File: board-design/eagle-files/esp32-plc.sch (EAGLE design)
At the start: 42 parts, among them P1 47346-0001, Q1 600mA/40V, Q2 600mA/40V, U1 ESP32-WROOM-32D, U2 FT231XS, U3 BD48E27G-TR, U5 EC20CEFASG-MINIPCIE

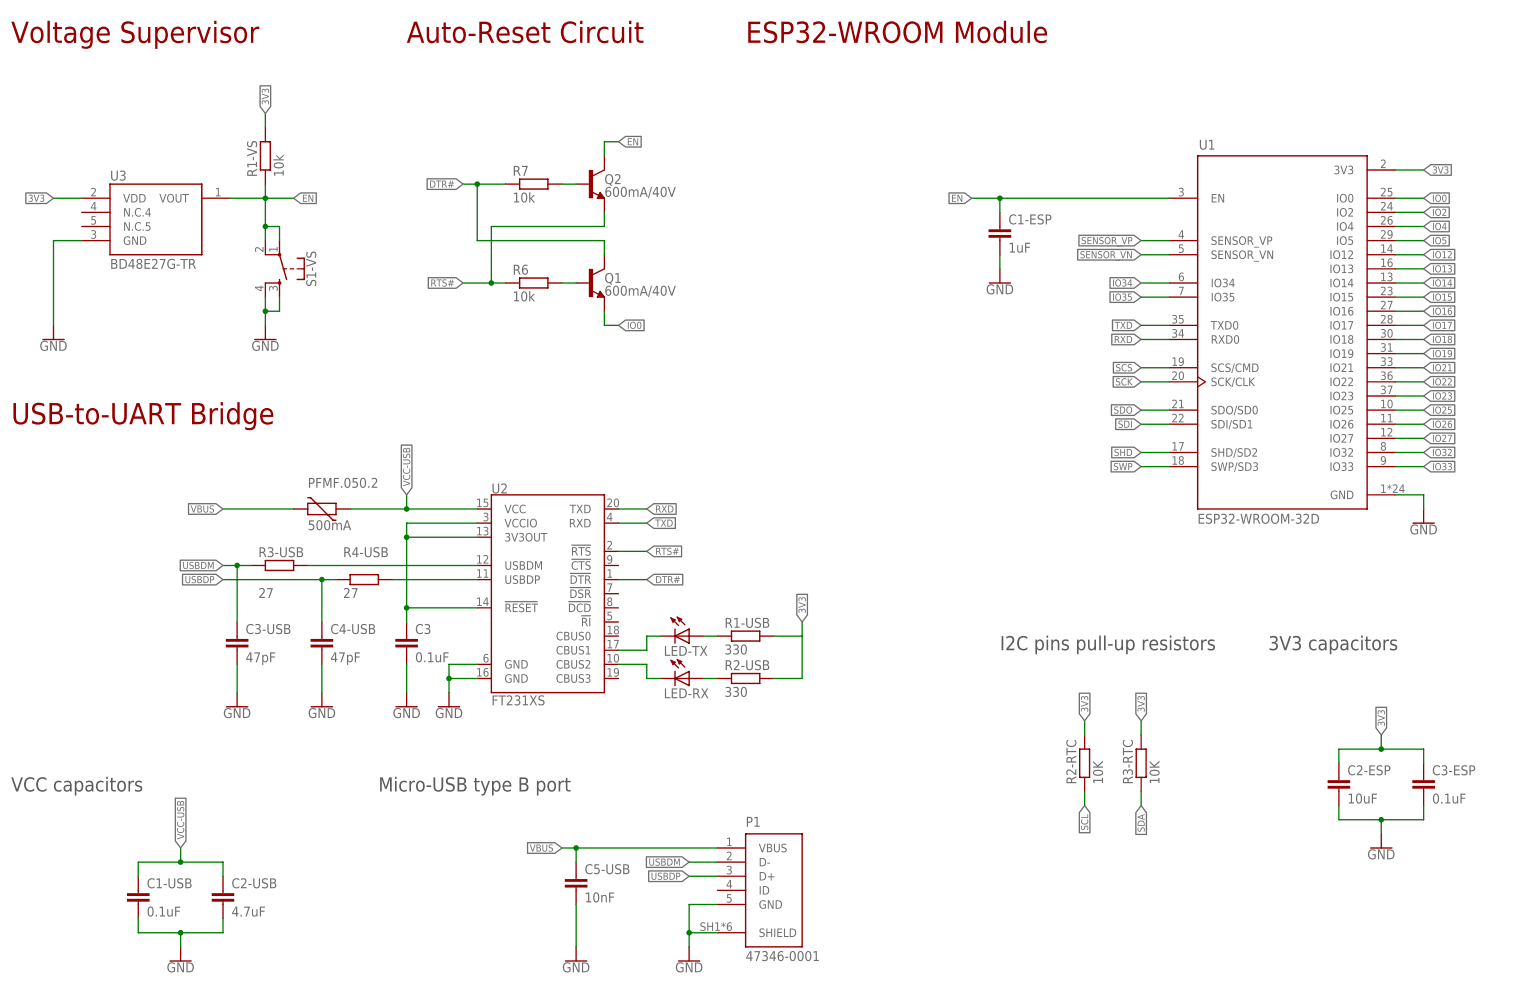
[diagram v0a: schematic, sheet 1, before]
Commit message: Changed board schematic
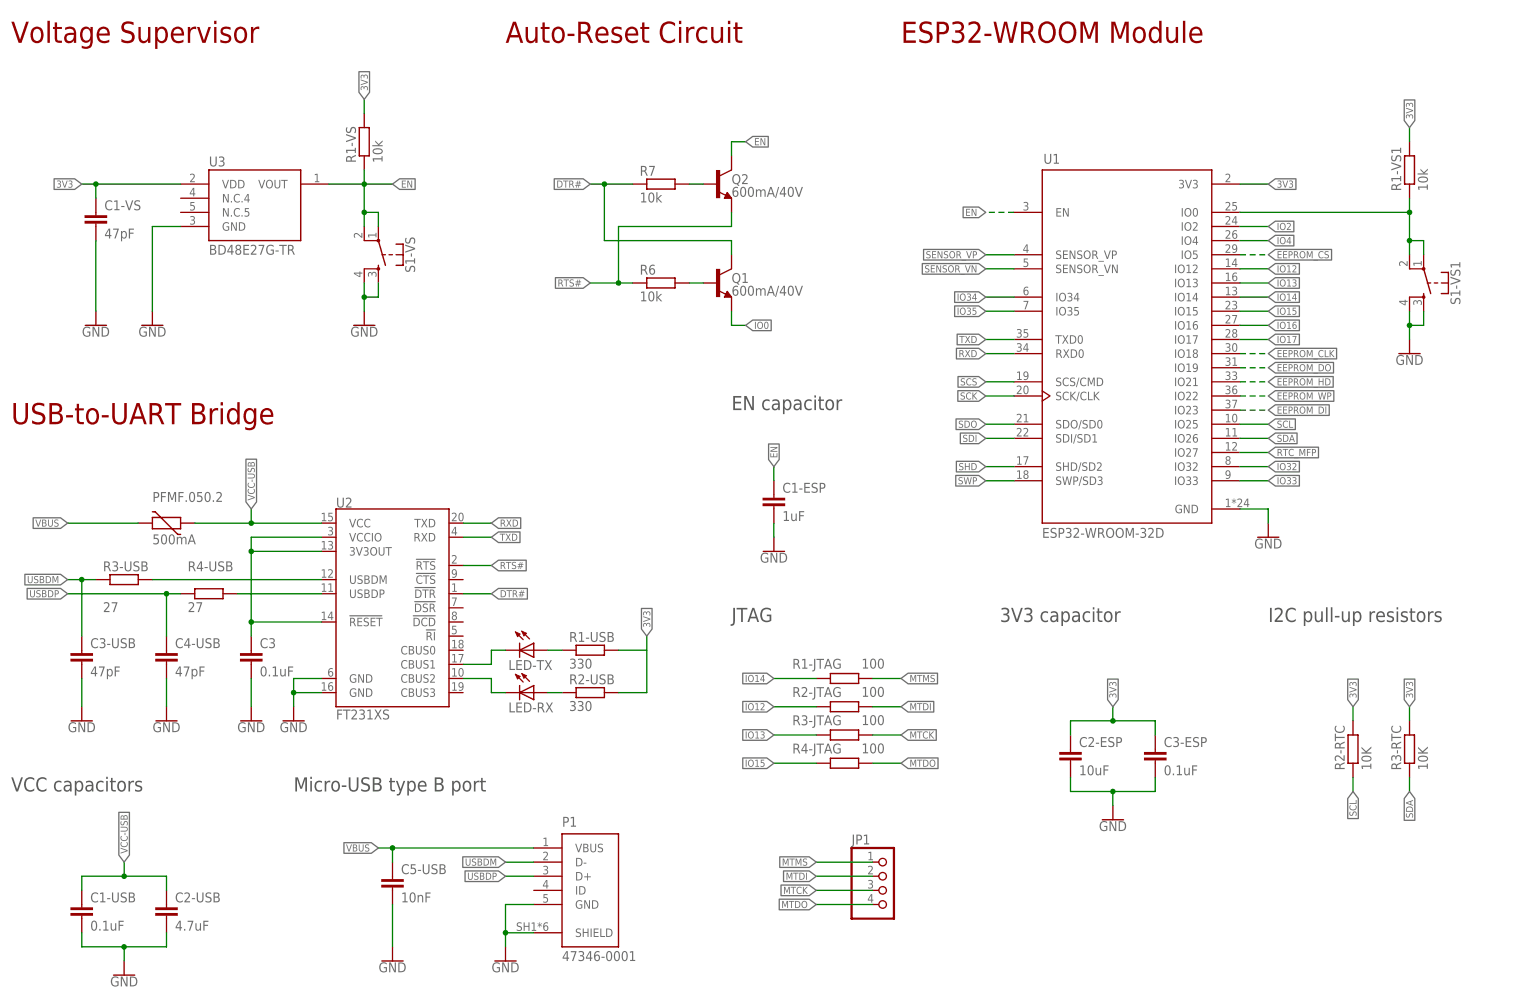
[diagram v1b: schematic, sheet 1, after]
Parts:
- removed C1-PWR: 100uF, rcl:C-EUC0402
- removed C2-PWR: 1000uF, rcl:C-EUC0402
- added C1-VS: 47pF, rcl:C-EUC0402
- added C2: 1000uF, cap-pan40:C-PR-5,0X10
- added C4: 100uF, cap-pan40:C-PR-5,0X10
- added JP1: (no value), pinhead:PINHD-1X4
- added R1-JTAG, R2-JTAG, R3-JTAG, R4-JTAG: 100, rcl:R-EU_R0402
- added R1-VS1: 10k, rcl:R-EU_R0402
- added S1-VS1: (no value), SparkFun-Switches:MOMENTARY-SWITCH-SPST-2-SMD-4.6X2.8MM
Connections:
- net N$14 renamed STATUS
- net N$15 renamed VBAT_BB
- net N$16 renamed VBAT_RF
- net N$17 renamed ANT_DIV
- net N$18 renamed ANT_MAIN
- net N$19 renamed ANT_GNSS
- net N$2 renamed USB_VBUS
- net N$20 renamed ADC0
- net N$21 renamed ADC1
- net N$22 renamed I2C_SDA
- net N$23 renamed I2C_SCL
- net N$24 renamed VDD_EXT
- net N$25 renamed AP_READY
- net N$26 renamed W_DISABLE#
- net N$27 renamed NET_MODE
- net N$28 renamed NET_STATUS
- net N$39 renamed WAKEUP_IN
- net N$40 renamed DBG_RXD
- net N$41 renamed DBG_TXD
- net N$42 renamed USIM_VDD
- net N$43 renamed USIM_GND
- net N$44 renamed USIM_DATA
- net N$45 renamed USIM_CLK
- net N$46 renamed USIM_RST
- net N$47 renamed RESET_IN
- net N$48 renamed PWRKEY
- net N$49 renamed PCM_IN
- net N$5 renamed USB_DM
- net N$50 renamed PCM_OUT
- net N$51 renamed PCM_SYNC
- net N$52 renamed PCM_CLK
- net N$53 renamed RESERVED
- net N$6 renamed USB_DP
- removed net IO18: U1.IO18
- removed net IO19: U1.IO19
- removed net IO21: U1.IO21
- removed net IO22: U1.IO22
- removed net IO23: U1.IO23
- removed net IO25: U1.IO25
- removed net IO26: U1.IO26
- removed net IO27: U1.IO27
- removed net IO5: U1.IO5
- removed net N$54: U5.GND
- new net MTCK: JP1.3, R3-JTAG.2
- new net MTDI: JP1.2, R2-JTAG.2
- new net MTDO: JP1.4, R4-JTAG.2
- new net MTMS: JP1.1, R1-JTAG.2
- new net VIN: C4.+, U$2.VIN
- net 3V3: now also C1-VS.1, C2.+, R1-VS1.2; no longer C2-PWR.1
- net EEPROM_CLK: now also U1.IO18
- net EEPROM_CS: now also U1.IO5
- net EEPROM_DI: now also U1.IO23
- net EEPROM_DO: now also U1.IO19
- net EEPROM_HD: now also U1.IO21
- net EEPROM_WP: now also U1.IO22
- net GND: now also C1-VS.2, C2.-, C4.-, S1-VS1.3, S1-VS1.4, U5.GND; no longer C1-PWR.2, C2-PWR.2
- net IO0: no longer U1.IO0
- net IO12: now also R2-JTAG.1
- net IO13: now also R3-JTAG.1
- net IO14: now also R1-JTAG.1
- net IO15: now also R4-JTAG.1
- net N$1: now also R1-VS1.1, S1-VS1.1, S1-VS1.2, U1.IO0; no longer C1-PWR.1, U$2.VIN
- net RTC_MFP: now also U1.IO27
- net SCL: now also U1.IO25
- net SDA: now also U1.IO26
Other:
- note added: "3V3 capacitor"
- note added: "EC20 LTE Cat 4 Module"
- note added: "EN capacitor"
- note added: "I2C pull-up resistors"
- note added: "JTAG"
- note added: "Transistor / IC translation for UART communication required (IC translation recommended - IC needed) Further footprint checks required (2019 hardware manual for reference) Version R2.1: https://ro.mouser.com/datasheet/2/1052/Quectel_EC20_R2.1_LTE_Specification_V1.2-1830665.pdf"
- note removed: "3V3 capacitors"
- note removed: "I2C pins pull-up resistors"
- moved on the sheet: C1-EEPROM, C1-ESP, C1-USB, C2-ESP, C2-USB, C3, C3-ESP, C3-USB, C4-USB, C5-USB, LED-RX, LED-TX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

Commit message: Eagle schematic changed
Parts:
- removed C1-EEPROM, C3-RTC: 100nF, rcl:C-EUC0402
- removed C1-ESP: 1uF, rcl:C-EUC0402
- removed C1-RTC, C2-RTC: 5pF, rcl:C-EUC0402
- removed C1-USB, C3, C3-ESP: 0.1uF, rcl:C-EUC0402
- removed C1-VS, C3-USB, C4-USB: 47pF, rcl:C-EUC0402
- removed C2: 1000uF, cap-pan40:C-PR-5,0X10
- removed C2-ESP: 10uF, rcl:C-EUC0402
- removed C2-USB: 4.7uF, rcl:C-EUC0402
- removed C4: 100uF, cap-pan40:C-PR-5,0X10
- removed C5-USB: 10nF, rcl:C-EUC0402
- removed JP1: (no value), pinhead:PINHD-1X4
- removed LED-RX, LED-TX: (no value), adafruit:LEDCHIP-LED0603
- removed P1: 47346-0001, 47346-0001:47346-0001
- removed PFMF.050.2: 500mA, varistor:VARISTORCN1812
- removed R1-JTAG, R2-JTAG, R3-JTAG, R4-JTAG: 100, rcl:R-EU_R0402
- removed R1-USB, R2-USB: 330, rcl:R-EU_R0402
- removed R1-VS, R1-VS1, R6, R7: 10k, rcl:R-EU_R0402
- removed R2-RTC, R3-RTC: 10K, rcl:R-EU_R0402
- removed R3-USB, R4-USB: 27, rcl:R-EU_R0402
- removed S1-VS, S1-VS1: (no value), SparkFun-Switches:MOMENTARY-SWITCH-SPST-2-SMD-4.6X2.8MM
- removed U1: ESP32-WROOM-32D, ESP32-WROOM-32D:ESP32-WROOM-32D
- removed U2: FT231XS, SparkFun-IC-Comms:FT231XS
- removed U3: BD48E27G-TR, BD48E27G-TR:BD48E27G-TR
- removed U5: EC20CEFASG-MINIPCIE, Quectel:EC20CEFASG-MINIPCIE
- added C4-RTC: 100pF, rcl:C-EUC0402
- added D1: 24V, SparkFun-DiscreteSemi:DIODE_TVS
- added D2, D3: 3A/40V/500mV, SparkFun-DiscreteSemi:DIODE-SCHOTTKY-B340A
- added EEPROM-C1, EERAM-C1, ETH-VDD1A-C2, ETH-VDD2A-C2, ETH-VDDIO-C2, LTE-USIM-C1, LTE-VBAT-C2, LTE-VBAT-C6, PSU-OUT-C6, RTC-C1: 100nF, rcl:C-EUC0402
- added EERAM-C2: 33uF / 6.3V, rcl:C-EUC0402
- added ESP-C1: 22uF, rcl:C-EUC0402
- added ESP-C2: 0.1uF, rcl:C-EUC0402
- added ESP-C3, ETH-RJ45-C1, ETH-VDDCR-C1, VS-C1: 1uF, rcl:C-EUC0402
- added ESP-JTAG: (no value), pinhead:PINHD-1X4
- added ESP-R1, ESP-R2, ESP-R3, ESP-R4, ESP-R5, ESP-R6, ETH-RJ45-R10, ETH-RJ45-R9: 10k, rcl:R-EU_R0402
- added ESP-S1, ESP-S2: (no value), SparkFun-Switches:MOMENTARY-SWITCH-SPST-2-SMD-4.6X2.8MM
- added ESP-UART0: (no value), pinhead:PINHD-1X6
- added ETH-RJ45-R1, ETH-RJ45-R2, ETH-RJ45-R3, ETH-RJ45-R4: 49.9R, rcl:R-EU_R0402
- added ETH-RJ45-R5, ETH-RJ45-R6, R1-RTC1: 1k, rcl:R-EU_R0402
- added ETH-RJ45-R7: 12.1R (1%), rcl:R-EU_R0402
- added ETH-RJ45-R8: 500R, rcl:R-EU_R0402
- added ETH-VDD1A-C1, ETH-VDD2A-C1, PSU-IN-C3: 10uF, rcl:C-EUC0402
- added ETH-VDD2A-C3, ETH-VDD2A-C4, ETH-VDD2A-C5: 20pF, rcl:C-EUC0402
- added ETH-VDDCR-C2: 470pF, rcl:C-EUC0402
- added ETH-VDDIO-C1, LTE-VBAT-C10, LTE-VBAT-C9, PSU-OUT-C3: 22uF, rcl:CPOL-EUC/6032-28R
- added FB1: 30Ω/1.8A, SparkFun-Coils:FERRITE_BEAD-0603
- added G1: CR2032H, battery:CR2032H
- added L1: 330uH, rcl:L-EUL1812
- added L2, L3, L4: (no value), SparkFun-Coils:INDUCTOR
- added LTE-USIM-C2, LTE-USIM-C3, LTE-USIM-C4, LTE-VBAT-C3, LTE-VBAT-C7: 33pF, rcl:C-EUC0402
- added LTE-USIM-R1: 15K, rcl:R-EU_R0402
- added LTE-USIM-R2, LTE-USIM-R3, LTE-USIM-R4, PSU-OUT-R1: 0R, rcl:R-EU_R0402
- added LTE-VBAT-C1, LTE-VBAT-C11, LTE-VBAT-C5, PSU-OUT-C2: 100uF, rcl:CPOL-EUC/6032-28R
- added LTE-VBAT-C4, LTE-VBAT-C8: 10pF, rcl:C-EUC0402
- added PSU-IN-C1, PSU-IN-C2: 47uF, rcl:CPOL-EUC/6032-28R
- added PSU-OUT-C1: 10uF, rcl:CPOL-EUC/6032-28R
- added PSU-OUT-C4: 220uF, rcl:CPOL-EUC/6032-28R
- added PSU-OUT-C5: 470uF, rcl:CPOL-EUC/6032-28R
- added RTC-C2, RTC-C3: 15pF, rcl:C-EUC0402
- added U$10: ESDA6V1P6, my-STMicroelectronics:ESDA6V1P6
- added U$11: LAN8720A-CP, my-MicrochipTechnology:LAN8720A-CP
- added U$12: 7499010121A, my-WurthElektronik:7499010121A
- added U$7: BD48E30G-TR, my-ROHMSemiconductor:BD48E30G-TR
- added U$8: LM2576SX-3.3/NOPB, my-Texas-Instruments:LM2576SX-3.3/NOPB
- added U$9: 104224-0820, my-Molex:104224-0820
- added U$93: ECS-250-20-30B-AEN-TR, my-ECSInc:ECS-250-20-30B-AEN-TR
- U$1: value M95M01-DWDW3TP/K -> M95M01-DWMN3TP/K; device my-STM:M95M01-DWDW3TP/K -> my-STMicroelectronics:M95M01-DWMN3TP/K
- U$2: value LM2576HVSX-3.3/NOPB -> ESP32-WROVER-E/IE; device my-TI:LM2576HVSX-3.3/NOPB -> my-Espressif-Systems:ESP32-WROVER-E/IE
- U$3: value MCP7940M-I/SN -> MCP7940N-I/SN; device my-Microchip:MCP7940M-I/SN -> my-Microchip-Technology:MCP7940N-I/SN
- U$4: value FC-135-32.7680KA-AG0 -> ECS-.327-12.5-12QS-TR; device my-ET:FC-135-32.7680KA-AG0 -> my-ECSInc:ECS-.327-12.5-12QS-TR
- U$5: value V3PM6-M3/H -> 48L512T-I/SN; device my-Vishay:V3PM6-M3/H -> my-Microchip-Technology:48L512T-I/SN
- U$6: value SDR1005-101KL -> EC20CEFASG-MINIPCIE; device my-Bourns:SDR1005-101KL -> my-Quectel:EC20CEFASG-MINIPCIE
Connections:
- removed net 3V3: C1-EEPROM.1, C1-VS.1, C2-ESP.1, C2.+, C3-ESP.1, C3-RTC.1, R1-RTC.2, R1-VS.2, R1-VS1.2, R2-RTC.2, R2-USB.2, R3-RTC.2, U$1.VCC, U$2.FB, U$3.VCC, U$6.P$1, U1.3V3, U3.VDD
- removed net ADC0: U5.ADC0
- removed net ADC1: U5.ADC1
- removed net ANT_DIV: U5.ANT_DIV
- removed net ANT_GNSS: U5.ANT_GNSS
- removed net ANT_MAIN: U5.ANT_MAIN
- removed net AP_READY: U5.AP_READY
- removed net DBG_RXD: U5.DBG_RXD
- removed net DBG_TXD: U5.DBG_TXD
- removed net DTR#: Q1.C, R7.1, U2.!DTR
- removed net EEPROM_CLK: U$1.C, U1.IO18
- removed net EEPROM_CS: U$1.S#, U1.IO5
- removed net EEPROM_DI: U$1.D, U1.IO23
- removed net EEPROM_DO: U$1.Q, U1.IO19
- removed net EEPROM_HD: U$1.HOLD#, U1.IO21
- removed net EEPROM_WP: U$1.W#, U1.IO22
- removed net EN: C1-ESP.1, Q2.C, R1-VS.1, S1-VS.1, S1-VS.2, U1.EN, U3.VOUT
- removed net I2C_SCL: U5.I2C_SCL
- removed net I2C_SDA: U5.I2C_SDA
- removed net IO0: Q1.E
- removed net IO12: R2-JTAG.1, U1.IO12
- removed net IO13: R3-JTAG.1, U1.IO13
- removed net IO14: R1-JTAG.1, U1.IO14
- removed net IO15: R4-JTAG.1, U1.IO15
- removed net IO16: U1.IO16
- removed net IO17: U1.IO17
- removed net IO2: U1.IO2
- removed net IO32: U1.IO32
- removed net IO33: U1.IO33
- removed net IO34: U1.IO34
- removed net IO35: U1.IO35
- removed net IO4: U1.IO4
- removed net MTCK: JP1.3, R3-JTAG.2
- removed net MTDI: JP1.2, R2-JTAG.2
- removed net MTDO: JP1.4, R4-JTAG.2
- removed net MTMS: JP1.1, R1-JTAG.2
- removed net NET_MODE: U5.NET_MODE
- removed net NET_STATUS: U5.NET_STATUS
- removed net PCM_CLK: U5.PCM_CLK
- removed net PCM_IN: U5.PCM_IN
- removed net PCM_OUT: U5.PCM_OUT
- removed net PCM_SYNC: U5.PCM_SYNC
- removed net PWRKEY: U5.PWRKEY
- removed net RESERVED: U5.RESERVED
- removed net RESET_IN: U5.RESET_N
- removed net RTS#: Q2.E, R6.1, U2.!RTS
- removed net RXD: U1.RXD0, U2.TXD
- removed net SCK: U1.SCK/CLK
- removed net SCL: R2-RTC.1, U$3.SCL, U1.IO25
- removed net SCS: U1.SCS/CMD
- removed net SDA: R3-RTC.1, U$3.SDA, U1.IO26
- removed net SDI: U1.SDI/SD1
- removed net SDO: U1.SDO/SD0
- removed net SHD: U1.SHD/SD2
- removed net STATUS: U5.STATUS
- removed net SWP: U1.SWP/SD3
- removed net TXD: U1.TXD0, U2.RXD
- removed net USBDM: C3-USB.1, P1.D-, R3-USB.1
- removed net USBDP: C4-USB.1, P1.D+, R4-USB.1
- removed net USB_DM: U5.USB_DM
- removed net USB_DP: U5.USB_DP
- removed net USB_VBUS: U5.USB_VBUS
- removed net USIM_GND: U5.USIM_GND
- removed net USIM_VDD: U5.USIM_VDD
- removed net VBAT_BB: U5.VBAT_BB
- removed net VBAT_RF: U5.VBAT_RF
- removed net VBUS: C5-USB.1, P1.VBUS, PFMF.050.2.2
- removed net VCC-USB: C1-USB.1, C2-USB.1, PFMF.050.2.1, U2.VCC
- removed net VDD_EXT: U5.VDD_EXT
- removed net VIN: C4.+, U$2.VIN
- removed net WAKEUP_IN: U5.WAKEUP_IN
- removed net W_DISABLE#: U5.W_DISABLE#
- new net !ESP_DTR: ESP-R1.1, ESP-UART0.4, Q1.C
- new net !ESP_RST: ESP-UART0.5
- new net !ESP_RTS: ESP-R2.1, Q2.E
- new net 24V: FB1.1
- new net 3.3V: D1.C, EEPROM-C1.1, EERAM-C1.1, ESP-UART0.1, L2.1, L3.1, L4.1, PSU-OUT-C3.+, PSU-OUT-C4.+, PSU-OUT-C5.+, PSU-OUT-C6.1, PSU-OUT-R1.1, R1-RTC.2, RTC-C1.1, U$1.VCC, U$3.VCC, U$5.VCC, U$7.VDD, VS-C1.1
- new net EERAM_VCAP: EERAM-C2.1, U$5.VCAP
- new net ESP_3V3: ESP-C1.1, ESP-C2.1, ESP-R3.2, ESP-R4.2, ESP-R5.2, ESP-R6.2, L4.2, LTE-VBAT-C11.+, U$2.3V3
- new net ESP_BOOT: ESP-R4.1, ESP-S2.1, ESP-S2.2, Q1.E, U$2.IO0
- new net ESP_EN: ESP-C3.1, ESP-R3.1, ESP-S1.1, ESP-S1.2, Q2.C, U$2.EN, U$7.VOUT
- new net ESP_MTCK: ESP-JTAG.3, U$2.IO13
- new net ESP_MTDI: ESP-JTAG.2, U$2.IO12
- new net ESP_MTDO: ESP-JTAG.4, U$2.IO15
- new net ESP_MTMS: ESP-JTAG.1, U$2.IO14
- new net ESP_RXD0: ESP-UART0.3, U$2.RXD0
- new net ESP_SCL: ESP-R5.1, U$3.SCL
- new net ESP_SDA: ESP-R6.1, U$3.SDA
- new net ESP_TXD0: ESP-UART0.2, U$2.TXD0
- new net ESP_VSPICLK: U$2.IO18
- new net ESP_VSPICS: U$2.IO5
- new net ESP_VSPID: U$2.IO23
- new net ESP_VSPIHD: U$2.IO21
- new net ESP_VSPIQ: U$2.IO19
- new net ESP_VSPIWP: U$2.IO22
- new net ETH_NRST: ETH-RJ45-R9.1, ETH-VDD2A-C5.1, U$11.NRST
- new net ETH_RJ45_LED1: ETH-RJ45-R5.2, U$11.LED1/!REGOFF
- new net ETH_RJ45_LED2: ETH-RJ45-R10.2, ETH-RJ45-R6.2, U$11.LED2/!NINTSEL
- new net ETH_RJ45_RXN: ETH-RJ45-R4.2, U$11.RXN, U$12.RD-
- new net ETH_RJ45_RXP: ETH-RJ45-R3.2, U$11.RXP, U$12.RD+
- new net ETH_RJ45_TXN: ETH-RJ45-R2.2, U$11.TXN, U$12.TD-
- new net ETH_RJ45_TXP: ETH-RJ45-R1.2, U$11.TXP, U$12.TD+
- new net ETH_VDD: ETH-RJ45-C1.1, ETH-RJ45-R1.1, ETH-RJ45-R2.1, ETH-RJ45-R3.1, ETH-RJ45-R4.1, ETH-RJ45-R9.2, ETH-VDD1A-C1.1, ETH-VDD1A-C2.1, ETH-VDD2A-C1.1, ETH-VDD2A-C2.1, ETH-VDDIO-C1.+, ETH-VDDIO-C2.1, L2.2, U$11.VDD1A, U$11.VDD2A, U$11.VDDIO, U$12.RCT, U$12.TCT
- new net ETH_VDDCR: ETH-VDDCR-C1.1, ETH-VDDCR-C2.1, U$11.VDDCR
- new net ETH_XTAL1: ETH-VDD2A-C3.1, U$11.XTAL1/CLKIN, U$93.XTAL1
- new net ETH_XTAL2: ETH-RJ45-R8.1, U$11.XTAL2
- new net LTE_CTS: U$6.CTS
- new net LTE_DBG_RXD: U$6.DBG_RXD
- new net LTE_DBG_TXD: U$6.DBG_TXD
- new net LTE_DCD: U$6.DCD
- new net LTE_DTR: U$6.DTR
- new net LTE_RI: U$6.RI
- new net LTE_RTS: U$6.RTS
- new net LTE_RXD: U$6.RXD
- new net LTE_TXD: U$6.TXD
- new net LTE_USIM_CLK: LTE-USIM-R3.2, U$6.USIM_CLK
- new net LTE_USIM_DATA: LTE-USIM-R2.2, U$6.USIM_DATA
- new net LTE_USIM_GND: LTE-USIM-C1.1, U$6.USIM_GND, U$9.GND
- new net LTE_USIM_RST: LTE-USIM-R4.2, U$6.USIM_RST
- new net LTE_USIM_VDD: LTE-USIM-C1.2, LTE-USIM-R1.2, U$10.I/O1, U$6.USIM_VDD, U$9.VCC
- new net LTE_VBAT: L3.2, LTE-VBAT-C1.+, LTE-VBAT-C10.+, LTE-VBAT-C2.1, LTE-VBAT-C3.1, LTE-VBAT-C4.1, LTE-VBAT-C5.+, LTE-VBAT-C6.1, LTE-VBAT-C7.1, LTE-VBAT-C8.1, LTE-VBAT-C9.+
- new net N$14: U$2.IO27
- new net N$15: U$2.IO26
- new net N$16: U$2.IO25
- new net N$17: U$2.IO33
- new net N$18: U$2.IO32
- new net N$19: U$2.IO35
- new net N$2: U$5.SCK
- new net N$20: U$2.IO34
- new net N$21: U$5.SO
- new net N$22: L1.2, PSU-OUT-C1.+, PSU-OUT-C2.+, PSU-OUT-R1.2, U$8.FB
- new net N$23: D3.C, L1.1, U$8.VOUT
- new net N$25: ETH-RJ45-R7.2, U$11.RBIAS
- new net N$26: U$11.RXER/!PHYAD0
- new net N$27: U$2.IO4
- new net N$28: U$11.CRS_DV/!MODE2
- new net N$3: U$1.!HOLD
- new net N$39: U$11.RXD1/!MODE1
- new net N$40: U$11.RXD0/!MODE0
- new net N$42: U$11.NINT/REFCLKO
- new net N$44: ETH-RJ45-R8.2, ETH-VDD2A-C4.1, U$93.XTAL2
- new net N$5: U$1.D
- new net N$6: D2.C, R1-RTC1.2
- new net RTC_VBAT: C4-RTC.1, R1-RTC.1, R1-RTC1.1, U$3.VBAT
- new net USIM_I/O: LTE-USIM-C2.1, LTE-USIM-R1.1, LTE-USIM-R2.1, U$9.I/O
- net GND: now also C4-RTC.2, D1.A, D3.A, EEPROM-C1.2, EERAM-C1.2, EERAM-C2.2, ESP-C1.2, ESP-C2.2, ESP-C3.2, ESP-S1.3, ESP-S1.4, ESP-S2.3, ESP-S2.4, ESP-UART0.6, ETH-RJ45-C1.2, ETH-RJ45-R10.1, ETH-RJ45-R7.1, ETH-VDD1A-C1.2, ETH-VDD1A-C2.2, ETH-VDD2A-C1.2, ETH-VDD2A-C2.2, ETH-VDD2A-C3.2, ETH-VDD2A-C4.2, ETH-VDD2A-C5.2, ETH-VDDCR-C1.2, ETH-VDDCR-C2.2, ETH-VDDIO-C1.-, ETH-VDDIO-C2.2, G1.-, LTE-USIM-C2.2, LTE-USIM-C3.2, LTE-USIM-C4.2, LTE-VBAT-C1.-, LTE-VBAT-C10.-, LTE-VBAT-C11.-, LTE-VBAT-C2.2, LTE-VBAT-C3.2, LTE-VBAT-C4.2, LTE-VBAT-C5.-, LTE-VBAT-C6.2, LTE-VBAT-C7.2, LTE-VBAT-C8.2, LTE-VBAT-C9.-, PSU-IN-C1.-, PSU-IN-C2.-, PSU-IN-C3.2, PSU-OUT-C1.-, PSU-OUT-C2.-, PSU-OUT-C3.-, PSU-OUT-C4.-, PSU-OUT-C5.-, PSU-OUT-C6.2, RTC-C1.2, RTC-C2.2, RTC-C3.2, U$10.GND@1, U$10.GND@2, U$11.P_GND, U$12.8, U$12.GREEN-, U$12.SHIELD@1, U$12.SHIELD@2, U$12.YELLOW-, U$2.GND@1, U$2.GND@2, U$2.GND@3, U$2.P_GND, U$5.VSS, U$6.GND, U$7.GND, U$8.!ON!/OFF, U$8.GND, U$8.P_GND, U$93.GND, VS-C1.2; no longer C1-EEPROM.2, C1-ESP.2, C1-RTC.2, C1-USB.2, C1-VS.2, C2-ESP.2, C2-RTC.2, C2-USB.2, C2.-, C3-ESP.2, C3-RTC.2, C3-USB.2, C3.2, C4-USB.2, C4.-, C5-USB.2, P1.GND, P1.SHIELD, S1-VS.3, S1-VS.4, S1-VS1.3, S1-VS1.4, U$2.GND, U$2.ON#/OFF, U$2.TAB, U$5.1, U1.GND, U2.GND@16, U2.GND@6, U3.GND, U5.GND
- net N$1: now also U$5.!HOLD; no longer R1-VS1.1, S1-VS1.1, S1-VS1.2, U1.IO0
- net N$10: now also U$1.!W; no longer U5.RTS
- net N$11: now also U$5.SI; no longer U5.CTS
- net N$12: now also FB1.2, PSU-IN-C1.+, PSU-IN-C2.+, PSU-IN-C3.1, U$8.VIN; no longer U5.DCD
- net N$13: now also U$5.!CS; no longer U5.RI
- net N$29: now also ESP-R2.2; no longer R6.2
- net N$30: now also ESP-R1.2; no longer R7.2
- net N$31: now also U$2.IO2; no longer LED-TX.C, U2.CBUS1
- net N$32: now also U$11.MDIO; no longer LED-RX.C, U2.CBUS2
- net N$33: now also U$11.MDC; no longer R3-USB.2, U2.USBDM
- net N$34: now also U$11.TXEN; no longer R4-USB.2, U2.USBDP
- net N$35: now also U$11.TXD0; no longer C3.1, U2.!RESET, U2.3V3OUT, U2.VCCIO
- net N$36: now also ETH-RJ45-R5.1, U$12.GREEN+; no longer LED-TX.A, R1-USB.1
- net N$37: now also U$11.TXD1; no longer LED-RX.A, R2-USB.1
- net N$38: now also ETH-RJ45-R6.1, U$12.YELLOW+; no longer R1-USB.2
- net N$4: now also U$1.C; no longer U$2.VOUT, U$5.2, U$6.P$2
- net N$7: now also D2.A, G1.+; no longer U5.RXD
- net N$8: now also U$1.!S; no longer U5.TXD
- net N$9: now also U$1.Q; no longer U5.DTR
- net RTC_MFP: no longer R1-RTC.1, U1.IO27
- net RTC_X1: now also RTC-C2.1, U$4.P$1; no longer C1-RTC.1, U$4.2
- net RTC_X2: now also RTC-C3.1, U$4.P$2; no longer C2-RTC.1, U$4.1
- net SENSOR_VN: now also U$2.SENSOR_VN; no longer U1.SENSOR_VN
- net SENSOR_VP: now also U$2.SENSOR_VP; no longer U1.SENSOR_VP
- net USIM_CLK: now also LTE-USIM-C3.1, LTE-USIM-R3.1, U$10.I/O3, U$9.CLK; no longer U5.USIM_CLK
- net USIM_DATA: now also U$10.I/O4; no longer U5.USIM_DATA
- net USIM_RST: now also LTE-USIM-C4.1, LTE-USIM-R4.1, U$10.I/O2, U$9.RST; no longer U5.USIM_RST
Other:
- note added: "(U)SIM card holder"
- note added: "25MHz crystal"
- note added: "32kHz crystal"
- note added: "3V3 capacitors"
- note added: "Auto-reset circuit"
- note added: "Back-up supply"
- note added: "Boot & EN features"
- note added: "ESP-WROVER-IE"
- note added: "ETHERNET LM7820A"
- note added: "LTE EC20 R2.1"
- note added: "Notes: The cases of capacitors has to be determined, only the values being relevant at the moment. The cases and characteristics of inductors and diodes have yet to be determined. They were selected randomly for circuit showing purposes. This is a draft!"
- note added: "RJ45LAN transformer"
- note added: "SPI bus EEPROM"
- note added: "SPI bus EERAM"
- note added: "Step-down voltage regulator"
- note added: "Supply pins"
- note added: "Tantalum"
- note added: "UART interface circuit"
- note added: "UART0"
- note added: "VBAT capacitors"
- note added: "VDD capacitors"
- note added: "Voltage supervisor"
- note added: "nRST pull-up"
- note removed: "32kHz RTC crystal"
- note removed: "3V3 capacitor"
- note removed: "Auto-Reset Circuit"
- note removed: "EC20 LTE Cat 4 Module"
- note removed: "EN capacitor"
- note removed: "ESP32-WROOM Module"
- note removed: "MFP pull-up resistor"
- note removed: "Micro-USB type B port"
- note removed: "SPI Bus EEPROM"
- note removed: "Step-Down Voltage Regulator"
- note removed: "Transistor / IC translation for UART communication required (IC translation recommended - IC needed) Further footprint checks required (2019 hardware manual for reference) Version R2.1: https://ro.mouser.com/datasheet/2/1052/Quectel_EC20_R2.1_LTE_Specification_V1.2-1830665.pdf"
- note removed: "USB-to-UART Bridge"
- note removed: "VCC capacitors"
- note removed: "Voltage Supervisor"

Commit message: Added RS485 Interface Module
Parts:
- removed ETH-RJ45-C1, ETH-VDDCR-C1: 1uF, rcl:C-EUC0402
- removed ETH-RJ45-R1, ETH-RJ45-R2, ETH-RJ45-R3, ETH-RJ45-R4: 49.9R, rcl:R-EU_R0402
- removed ETH-RJ45-R10, ETH-RJ45-R9: 10k, rcl:R-EU_R0402
- removed ETH-RJ45-R5, ETH-RJ45-R6: 1k, rcl:R-EU_R0402
- removed ETH-RJ45-R7: 12.1R (1%), rcl:R-EU_R0402
- removed ETH-RJ45-R8: 500R, rcl:R-EU_R0402
- removed ETH-VDD1A-C1, ETH-VDD2A-C1: 10uF, rcl:C-EUC0402
- removed ETH-VDD1A-C2, ETH-VDD2A-C2, ETH-VDDIO-C2: 100nF, rcl:C-EUC0402
- removed ETH-VDD2A-C3, ETH-VDD2A-C4, ETH-VDD2A-C5: 20pF, rcl:C-EUC0402
- removed ETH-VDDCR-C2: 470pF, rcl:C-EUC0402
- removed ETH-VDDIO-C1: 22uF, rcl:CPOL-EUC/6032-28R
- removed L2: (no value), SparkFun-Coils:INDUCTOR
- removed U$12: 7499010121A, my-WurthElektronik:7499010121A
- removed U$93: ECS-250-20-30B-AEN-TR, my-ECSInc:ECS-250-20-30B-AEN-TR
- added EEPROM-C2, EERAM-C3, RS-C1, RTC-C4, VS-C2: 10uF, rcl:C-EUC0402
- added JP1, JP2: (no value), pinhead:PINHD-1X1
- added JP3: (no value), pinhead:PINHD-1X3
- added RS-C2: 100nF, rcl:C-EUC0402
- added RS-R1: 120, rcl:R-EU_R0402
- ESP-C2: value 0.1uF -> 100nF
- U$11: value LAN8720A-CP -> MAX3485CSA+T; device my-MicrochipTechnology:LAN8720A-CP -> my-MaximIntegrated:MAX3485CSA+T
- VS-C1: value 1uF -> 100nF
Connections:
- net N$1 renamed EERAM_HOLD
- net N$10 renamed EEPROM_W
- net N$11 renamed EERAM_SI
- net N$13 renamed EERAM_CS
- net N$2 renamed EERAM_SCK
- net N$21 renamed EERAM_SO
- net N$3 renamed EEPROM_HOLD
- net N$4 renamed EEPROM_C
- net N$5 renamed EEPROM_D
- net N$8 renamed EEPROM_S
- net N$9 renamed EEPROM_Q
- removed net ETH_NRST: ETH-RJ45-R9.1, ETH-VDD2A-C5.1, U$11.NRST
- removed net ETH_RJ45_LED1: ETH-RJ45-R5.2, U$11.LED1/!REGOFF
- removed net ETH_RJ45_LED2: ETH-RJ45-R10.2, ETH-RJ45-R6.2, U$11.LED2/!NINTSEL
- removed net ETH_RJ45_RXN: ETH-RJ45-R4.2, U$11.RXN, U$12.RD-
- removed net ETH_RJ45_RXP: ETH-RJ45-R3.2, U$11.RXP, U$12.RD+
- removed net ETH_RJ45_TXN: ETH-RJ45-R2.2, U$11.TXN, U$12.TD-
- removed net ETH_RJ45_TXP: ETH-RJ45-R1.2, U$11.TXP, U$12.TD+
- removed net ETH_VDD: ETH-RJ45-C1.1, ETH-RJ45-R1.1, ETH-RJ45-R2.1, ETH-RJ45-R3.1, ETH-RJ45-R4.1, ETH-RJ45-R9.2, ETH-VDD1A-C1.1, ETH-VDD1A-C2.1, ETH-VDD2A-C1.1, ETH-VDD2A-C2.1, ETH-VDDIO-C1.+, ETH-VDDIO-C2.1, L2.2, U$11.VDD1A, U$11.VDD2A, U$11.VDDIO, U$12.RCT, U$12.TCT
- removed net ETH_VDDCR: ETH-VDDCR-C1.1, ETH-VDDCR-C2.1, U$11.VDDCR
- removed net ETH_XTAL1: ETH-VDD2A-C3.1, U$11.XTAL1/CLKIN, U$93.XTAL1
- removed net ETH_XTAL2: ETH-RJ45-R8.1, U$11.XTAL2
- removed net N$32: U$11.MDIO
- removed net N$33: U$11.MDC
- removed net N$34: U$11.TXEN
- removed net N$35: U$11.TXD0
- removed net N$36: ETH-RJ45-R5.1, U$12.GREEN+
- removed net N$37: U$11.TXD1
- removed net N$38: ETH-RJ45-R6.1, U$12.YELLOW+
- removed net N$39: U$11.RXD1/!MODE1
- removed net N$40: U$11.RXD0/!MODE0
- removed net N$42: U$11.NINT/REFCLKO
- removed net N$44: ETH-RJ45-R8.2, ETH-VDD2A-C4.1, U$93.XTAL2
- new net N$24: U$3.SCL
- new net P$1: JP3.3
- new net RS-DE: U$11.DE
- new net RS-DI: U$11.DI
- new net RS-RE: U$11.!RE
- new net RS-RO: U$11.RO
- new net V_IN: JP3.1
- net 3.3V: now also EEPROM-C2.1, EERAM-C3.1, RS-C1.1, RS-C2.1, RTC-C4.1, U$11.VCC, VS-C2.1; no longer L2.1
- net ESP_SCL: no longer U$3.SCL
- net ESP_SDA: no longer U$3.SDA
- net GND: now also EEPROM-C2.2, EERAM-C3.2, JP3.2, RS-C1.2, RS-C2.2, RTC-C4.2, U$11.GND, VS-C2.2; no longer ETH-RJ45-C1.2, ETH-RJ45-R10.1, ETH-RJ45-R7.1, ETH-VDD1A-C1.2, ETH-VDD1A-C2.2, ETH-VDD2A-C1.2, ETH-VDD2A-C2.2, ETH-VDD2A-C3.2, ETH-VDD2A-C4.2, ETH-VDD2A-C5.2, ETH-VDDCR-C1.2, ETH-VDDCR-C2.2, ETH-VDDIO-C1.-, ETH-VDDIO-C2.2, U$11.P_GND, U$12.8, U$12.GREEN-, U$12.SHIELD@1, U$12.SHIELD@2, U$12.YELLOW-, U$93.GND
- net LTE_VBAT: now also U$6.VBAT_BB, U$6.VBAT_RF
- net N$25: now also U$3.SDA; no longer ETH-RJ45-R7.2, U$11.RBIAS
- net N$26: now also JP1.1, RS-R1.1, U$11.B; no longer U$11.RXER/!PHYAD0
- net N$28: now also JP2.1, RS-R1.2, U$11.A; no longer U$11.CRS_DV/!MODE2
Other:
- note added: "Module in progress. Surge protection for very high currents and voltages required."
- note added: "RS-422/RS-485 Interface IC"
- note removed: "25MHz crystal"
- note removed: "ETHERNET LM7820A"
- note removed: "RJ45LAN transformer"
- note removed: "VDD capacitors"
- note removed: "nRST pull-up"
- moved on the sheet: D1, D2, G1, L3, U$1, U$10, U$3, U$4, U$5, U$6, U$7

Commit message: Updated schematic
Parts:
- removed JP1, JP2: (no value), pinhead:PINHD-1X1
- added C1: 1nF/1kV, rcl:C-EUC0805
- added D4: Green, SparkFun-LED:LED-YELLOW0603
- added D5: 36V, SparkFun-DiscreteSemi:DIODE-ZENER-BZT52C3V6S
- added D6: 0.5A/40V/420mV, SparkFun-DiscreteSemi:DIODE-SCHOTTKY-PMEG4005EJ
- added F1: 750mA, adafruit:PTCFUSE-1206
- added JP4: (no value), pinhead:PINHD-1X2
- added LTE-UART-R1, LTE-UART-R10, LTE-UART-R4, LTE-UART-R6, LTE-UART-R8, PSU-OUT-R3: 10K, rcl:R-EU_R0402
- added LTE-UART-R2, LTE-UART-R3, LTE-UART-R5, LTE-UART-R7, LTE-UART-R9: 4.7K, rcl:R-EU_R0402
- added LTE-VBAT-C12, LTE-VBAT-C13, LTE-VBAT-C14, LTE-VBAT-C15, LTE-VBAT-C16: 1nF, rcl:C-EUC0402
- added PSU-OUT-R2: 330, rcl:R-EU_R0402
- added PSU-OUT-R4: 1K, rcl:R-EU_R0402
- added Q3, Q4, Q5, Q6, Q7, Q8: 500mA/300V, SparkFun-DiscreteSemi:TRANS_NPN-MMBTA42
- added R1: 42/2kV, rcl:R-EU_R0805
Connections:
- removed net LTE_CTS: U$6.CTS
- removed net LTE_DCD: U$6.DCD
- removed net LTE_RTS: U$6.RTS
- removed net N$26: JP1.1, RS-R1.1, U$11.B
- removed net V_IN: JP3.1
- new net LTE_AP_READY: LTE-UART-R10.1, Q7.C, U$6.AP_READY
- new net LTE_VDD_EXT: LTE-UART-R1.2, LTE-UART-R10.2, LTE-UART-R2.2, LTE-UART-R3.2, LTE-UART-R5.2, LTE-UART-R6.2, LTE-UART-R7.2, LTE-UART-R9.2, LTE-VBAT-C12.2, LTE-VBAT-C13.2, LTE-VBAT-C14.2, LTE-VBAT-C15.2, LTE-VBAT-C16.2, U$6.VDD_EXT
- new net MCU_EINT: LTE-UART-R8.1, Q6.C
- new net MCU_GPIO0: Q5.E
- new net MCU_GPIO1: Q7.E
- new net MCU_RXD: LTE-UART-R4.1, Q4.C
- new net MCU_TXD: Q3.E
- new net N$1: LTE-UART-R5.1, LTE-VBAT-C14.1, Q5.B
- new net N$10: F1.2, JP3.2
- new net N$11: LTE-UART-R7.1, LTE-VBAT-C15.1, Q6.B
- new net N$13: D6.A, F1.1
- new net N$2: LTE-UART-R2.1, LTE-VBAT-C12.1, Q3.B
- new net N$3: LTE-UART-R3.1, LTE-VBAT-C13.1, Q4.B
- new net N$32: JP4.1, RS-R1.1, U$11.B
- new net N$4: D4.C, Q8.C
- new net N$5: D4.A, PSU-OUT-R2.2
- new net N$8: LTE-UART-R9.1, LTE-VBAT-C16.1, Q7.B
- new net N$9: PSU-OUT-R3.2, PSU-OUT-R4.1, Q8.B
- new net PSU_PWR_LED: PSU-OUT-R4.2
- net 24V: now also D5.C, D6.C
- net 3.3V: now also LTE-UART-R4.2, LTE-UART-R8.2, PSU-OUT-R2.1, PSU-OUT-R3.1
- net GND: now also C1.1, D5.A, JP3.3, Q8.E, R1.2; no longer JP3.2
- net LTE_DTR: now also LTE-UART-R6.1, Q5.C
- net LTE_RI: now also Q6.E
- net LTE_RXD: now also LTE-UART-R1.1, Q3.C
- net LTE_TXD: now also Q4.E
- net N$28: now also JP4.2; no longer JP2.1
- net P$1: now also C1.2, JP3.1, R1.1; no longer JP3.3
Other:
- note added: "ESP32 - EC20 UART connection: EC20 ESP32 ___________ ___________ RXD <- - - - - - - - - - TXD TXD - - - - - - - - - -> RXD RI - - - - - - - - - -> EINT DTR <- - - - - - - - - - GPIO AP_READY <- - - - - - - - - - GPIO GND - - - - - - - - - - - GND"
- note added: "Power LED"
- note added: "Surge protection"
- note removed: "Module in progress. Surge protection for very high currents and voltages required."
- moved on the sheet: D1, FB1, JP3, L3, U$1, U$10, U$11, U$5, U$8, U$9
